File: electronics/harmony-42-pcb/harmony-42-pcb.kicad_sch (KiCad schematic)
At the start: 12 parts

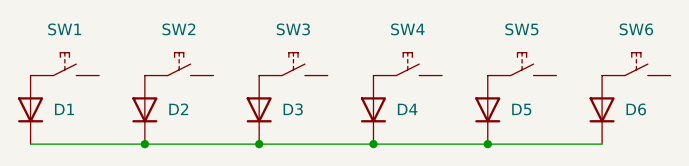
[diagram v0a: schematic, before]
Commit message: Add diodes
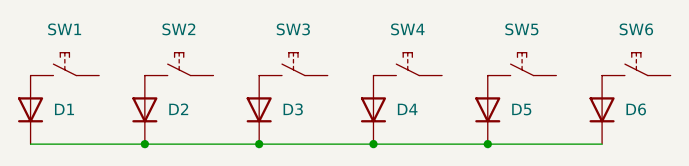
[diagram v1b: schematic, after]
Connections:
- net at SW4.1: no longer D4.2 (A)
- net at SW4.2: now also D4.2 (A)
- net at D5.2 (A): now also SW5.2; no longer SW5.1
- net at SW3.1: no longer D3.2 (A)
- net at SW3.2: now also D3.2 (A)
- net at SW6.1: no longer D6.2 (A)
- net at SW6.2: now also D6.2 (A)
- net at D1.2 (A): now also SW1.2; no longer SW1.1
- net at D2.2 (A): now also SW2.2; no longer SW2.1
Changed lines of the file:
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@@
 		(lib_id "Project_Library:SW_Hot_Swap_Socket")
 		(at 64.77 22.86 0)
+		(mirror y)
 		(unit 1)
 		(exclude_from_sim no)
@@
 		(lib_id "Project_Library:SW_Hot_Swap_Socket")
 		(at 52.07 22.86 0)
+		(mirror y)
 		(unit 1)
 		(exclude_from_sim no)
@@
 		(lib_id "Project_Library:SW_Hot_Swap_Socket")
 		(at 77.47 22.86 0)
+		(mirror y)
 		(unit 1)
 		(exclude_from_sim no)
@@
 		(lib_id "Project_Library:SW_Hot_Swap_Socket")
 		(at 90.17 22.86 0)
+		(mirror y)
 		(unit 1)
 		(exclude_from_sim no)
@@
 		(lib_id "Project_Library:SW_Hot_Swap_Socket")
 		(at 26.67 22.86 0)
+		(mirror y)
 		(unit 1)
 		(exclude_from_sim no)
@@
 		(lib_id "Project_Library:SW_Hot_Swap_Socket")
 		(at 39.37 22.86 0)
-		(unit 1)
-		(exclude_from_sim no)
+		(mirror y)
+		(unit 1)
+		(exclude_from_sim no)

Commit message: Add keys
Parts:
- added D10, D11, D12, D13, D14, D15, D16, D17, D18, D19, D20, D21, D22, D23, D24, D7, D8, D9: 1N4148WS, Project_Library:D_SOD-323F, symbol Diode:1N4148WS
- added SW10, SW11, SW12, SW13, SW14, SW15, SW16, SW17, SW18, SW19, SW20, SW21, SW22, SW23, SW24, SW7, SW8, SW9: ~, Project_Library:Hot_Swap_Socket_CPG151101S11, symbol Project_Library:SW_Hot_Swap_Socket
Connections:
- net at D1.1 (K), D2.1 (K), D3.1 (K)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: now also D10.1 (K), D11.1 (K), D12.1 (K), D7.1 (K), D8.1 (K), D9.1 (K)
- new net: D13.1 (K), D14.1 (K), D15.1 (K), D16.1 (K), D17.1 (K), D18.1 (K), D19.1 (K), D20.1 (K), D21.1 (K), D22.1 (K), D23.1 (K), D24.1 (K)
- new net: D24.2 (A), SW24.2
- new net: D22.2 (A), SW22.2
- new net: D23.2 (A), SW23.2
- new net: D21.2 (A), SW21.2
- new net: D12.2 (A), SW12.2
- new net: D11.2 (A), SW11.2
- new net: D20.2 (A), SW20.2
- new net: D8.2 (A), SW8.2
- new net: D15.2 (A), SW15.2
- new net: D7.2 (A), SW7.2
- new net: D13.2 (A), SW13.2
- new net: D19.2 (A), SW19.2
- new net: D10.2 (A), SW10.2
- new net: D9.2 (A), SW9.2
- new net: D16.2 (A), SW16.2
- new net: D14.2 (A), SW14.2
- new net: D17.2 (A), SW17.2
- new net: D18.2 (A), SW18.2

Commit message: Add keys
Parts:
- added D25, D26, D27, D28, D29, D30, D31, D32, D33, D34, D35, D36, D37, D38, D39, D40, D41, D42: 1N4148WS, Project_Library:D_SOD-323F, symbol Diode:1N4148WS
- added SW25, SW26, SW27, SW28, SW29, SW30, SW31, SW32, SW33, SW34, SW35, SW36, SW37, SW38, SW39, SW40, SW41, SW42: ~, Project_Library:Hot_Swap_Socket_CPG151101S11, symbol Project_Library:SW_Hot_Swap_Socket
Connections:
- new net: D25.1 (K), D26.1 (K), D27.1 (K), D28.1 (K), D29.1 (K), D30.1 (K), D31.1 (K), D32.1 (K), D33.1 (K), D34.1 (K), D35.1 (K), D36.1 (K)
- new net: D31.2 (A), SW31.2
- new net: D34.2 (A), SW34.2
- new net: D38.2 (A), SW38.2
- new net: D27.2 (A), SW27.2
- new net: D28.2 (A), SW28.2
- new net: D37.1 (K), D38.1 (K), D39.1 (K), D40.1 (K), D41.1 (K), D42.1 (K)
- new net: D40.2 (A), SW40.2
- new net: D41.2 (A), SW41.2
- new net: D33.2 (A), SW33.2
- new net: D42.2 (A), SW42.2
- new net: D29.2 (A), SW29.2
- new net: D30.2 (A), SW30.2
- new net: D32.2 (A), SW32.2
- new net: D36.2 (A), SW36.2
- new net: D39.2 (A), SW39.2
- new net: D26.2 (A), SW26.2
- new net: D37.2 (A), SW37.2
- new net: D25.2 (A), SW25.2
- new net: D35.2 (A), SW35.2

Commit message: Move diodes
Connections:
- net at SW4.1: now also SW16.1, SW28.1, SW37.1
- net at SW34.1: now also SW10.1, SW22.1
- net at SW38.1: now also SW17.1, SW29.1, SW5.1
- net at SW23.1: now also SW11.1, SW35.1
- net at SW3.1: now also SW15.1, SW27.1
- net at SW41.1: now also SW20.1, SW32.1, SW8.1
- net at SW33.1: now also SW21.1, SW42.1, SW9.1
- net at SW12.1: now also SW24.1, SW36.1
- net at SW6.1: now also SW18.1, SW30.1, SW39.1
- net at SW26.1: now also SW14.1, SW2.1
- net at SW13.1: now also SW1.1, SW25.1
- net at SW31.1: now also SW19.1, SW40.1, SW7.1

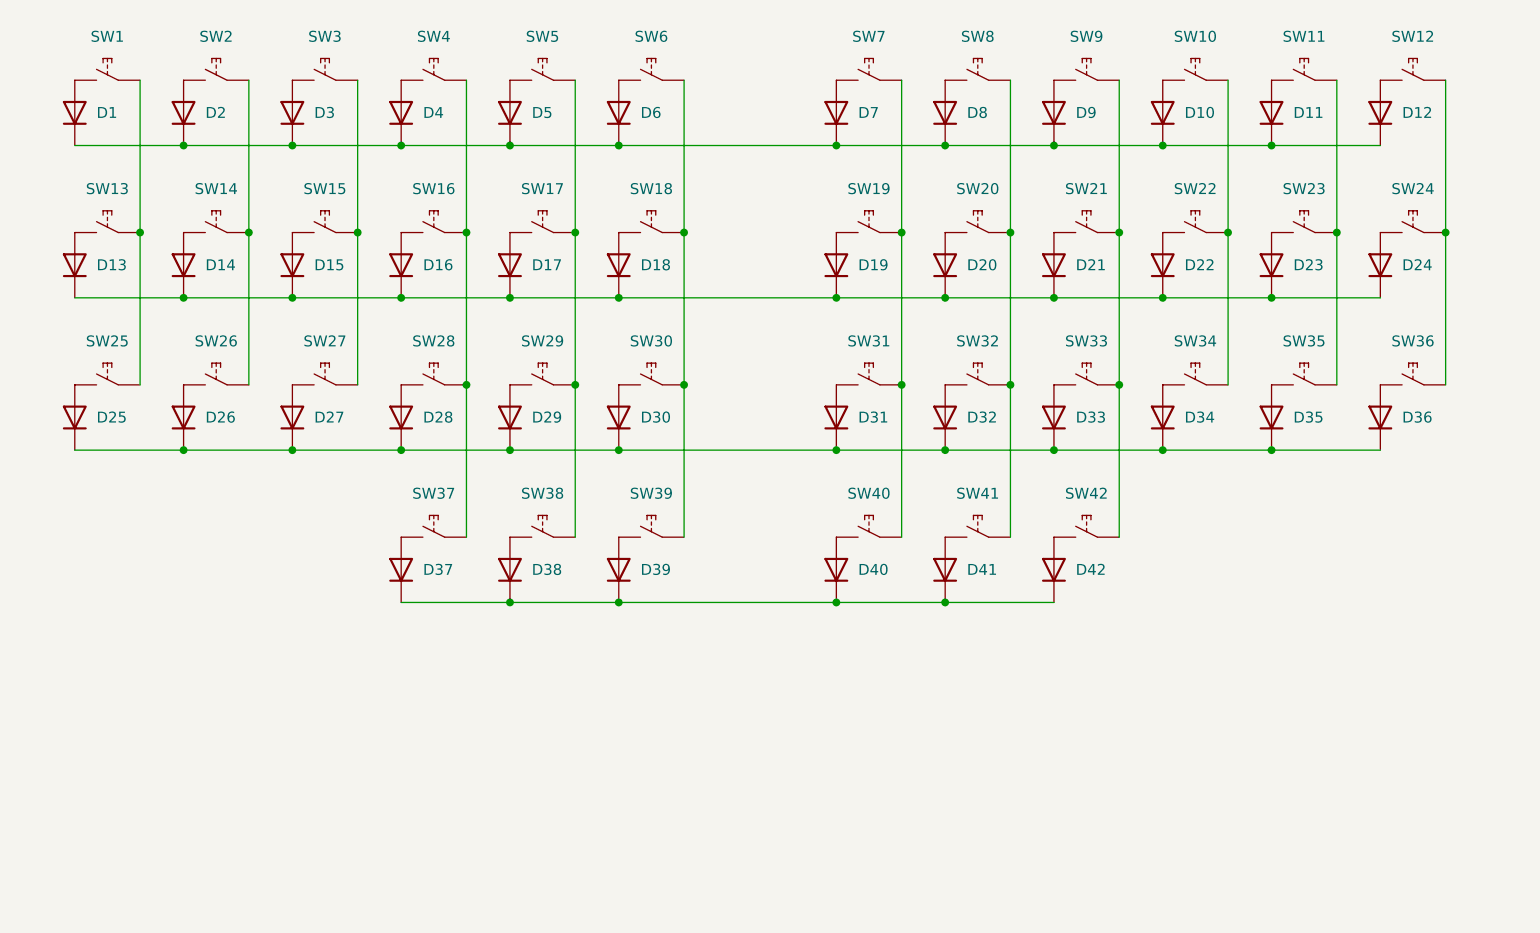
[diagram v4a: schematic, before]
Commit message: Add routes
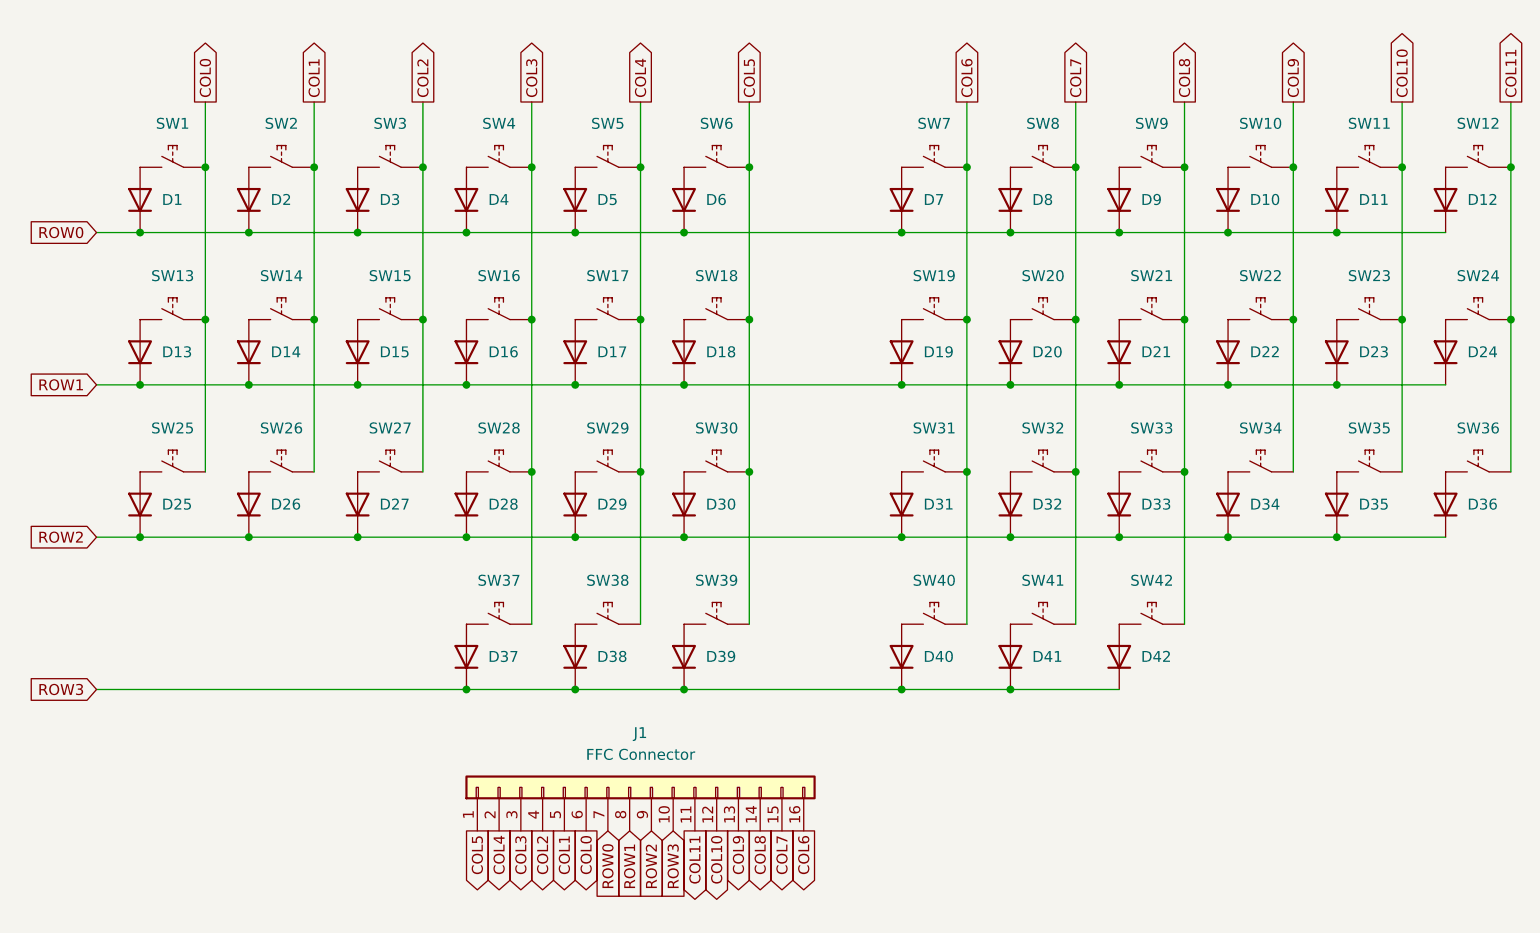
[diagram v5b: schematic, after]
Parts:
- added J1: FFC Connector, Project_Library:JUSHUO_AFC01-S16FCC-00, symbol Connector_Generic:Conn_01x16
- renumbered D39 to D37, D37 to D39
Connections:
- net ROW2: now reaches D25.1 (K), D26.1 (K), D27.1 (K), D28.1 (K), D29.1 (K), D30.1 (K), D31.1 (K), D32.1 (K), D33.1 (K), D34.1 (K), D35.1 (K), D36.1 (K)
- net ROW2: now also J1.9 (Pin_9)
- net ROW1: now reaches D13.1 (K), D14.1 (K), D15.1 (K), D16.1 (K), D17.1 (K), D18.1 (K), D19.1 (K), D20.1 (K), D21.1 (K), D22.1 (K), D23.1 (K), D24.1 (K)
- net ROW1: now also J1.8 (Pin_8)
- net COL3: now reaches SW16.1, SW28.1, SW37.1, SW4.1
- net COL3: now also J1.3 (Pin_3)
- net COL9: now reaches SW10.1, SW22.1, SW34.1
- net COL9: now also J1.13 (Pin_13)
- net COL4: now reaches SW17.1, SW29.1, SW38.1, SW5.1
- net COL4: now also J1.2 (Pin_2)
- net ROW0: now reaches D1.1 (K), D10.1 (K), D11.1 (K), D12.1 (K), D2.1 (K), D3.1 (K), D4.1 (K), D5.1 (K), D6.1 (K), D7.1 (K), D8.1 (K), D9.1 (K)
- net ROW0: now also J1.7 (Pin_7)
- net COL10: now reaches SW11.1, SW23.1, SW35.1
- net COL10: now also J1.12 (Pin_12)
- net COL2: now reaches SW15.1, SW27.1, SW3.1
- net COL2: now also J1.4 (Pin_4)
- net ROW3: now reaches D37.1 (K), D38.1 (K), D39.1 (K), D40.1 (K), D41.1 (K), D42.1 (K)
- net ROW3: now also J1.10 (Pin_10)
- net COL7: now reaches SW20.1, SW32.1, SW41.1, SW8.1
- net COL7: now also J1.15 (Pin_15)
- net COL8: now reaches SW21.1, SW33.1, SW42.1, SW9.1
- net COL8: now also J1.14 (Pin_14)
- net COL11: now reaches SW12.1, SW24.1, SW36.1
- net COL11: now also J1.11 (Pin_11)
- net COL5: now reaches SW18.1, SW30.1, SW39.1, SW6.1
- net COL5: now also J1.1 (Pin_1)
- net at D37.2 (A): now also SW37.2; no longer SW39.2
- net COL1: now reaches SW14.1, SW2.1, SW26.1
- net COL1: now also J1.5 (Pin_5)
- net at D39.2 (A): now also SW39.2; no longer SW37.2
- net COL0: now reaches SW1.1, SW13.1, SW25.1
- net COL0: now also J1.6 (Pin_6)
- net COL6: now reaches SW19.1, SW31.1, SW40.1, SW7.1
- net COL6: now also J1.16 (Pin_16)
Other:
- moved on the sheet: D1, D10, D11, D12, D13, D14, D15, D16, D17, D18, D19, D2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

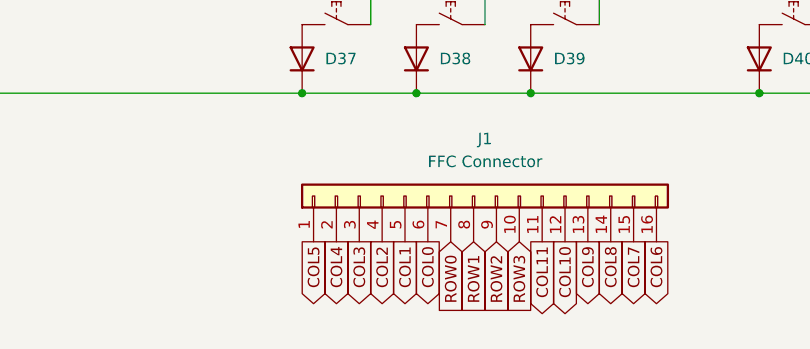
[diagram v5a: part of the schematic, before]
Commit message: Add routes
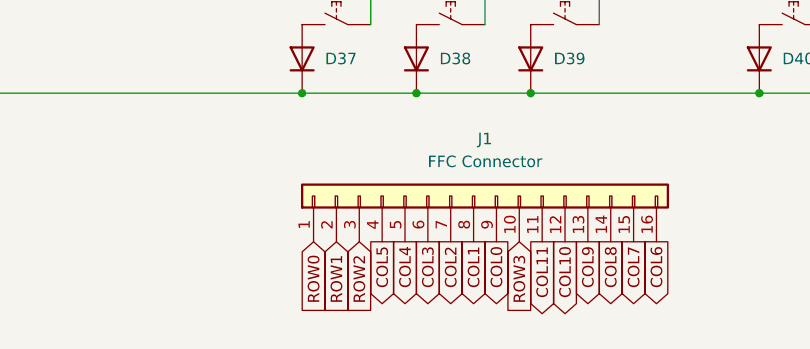
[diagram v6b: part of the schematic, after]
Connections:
- net COL0: now also J1.9 (Pin_9); no longer J1.6 (Pin_6)
- net COL1: now also J1.8 (Pin_8); no longer J1.5 (Pin_5)
- net COL2: now also J1.7 (Pin_7); no longer J1.4 (Pin_4)
- net COL3: now also J1.6 (Pin_6); no longer J1.3 (Pin_3)
- net COL4: now also J1.5 (Pin_5); no longer J1.2 (Pin_2)
- net COL5: now also J1.4 (Pin_4); no longer J1.1 (Pin_1)
- net ROW0: now also J1.1 (Pin_1); no longer J1.7 (Pin_7)
- net ROW1: now also J1.2 (Pin_2); no longer J1.8 (Pin_8)
- net ROW2: now also J1.3 (Pin_3); no longer J1.9 (Pin_9)
